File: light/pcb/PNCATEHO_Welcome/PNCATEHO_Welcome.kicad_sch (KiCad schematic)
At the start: 51 parts, among them J1 USB_C_Receptacle_USB2.0, SW11 Boot, SW12 Reset, U1 RP2040, U2 RT9013-33GB, U3 W25Q32JVSSIQ, U4 USBLC6-2SC6, Y1 12MHz

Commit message: clear sch
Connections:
- net RP2040_D+: no longer names the net of R6.2, U1.47 (USB_DP)
- net RP2040_D-: no longer names the net of R7.2, U1.46 (USB_DM)
- net USB_PROTECTED_D+ renamed USB_DP
- net USB_PROTECTED_D- renamed USB_DM
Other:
- note added: "Button"
- note added: "Decoupling capacitor"
- note added: "ESD"
- note added: "Flash"
- note added: "MCU Led"
- note added: "Test Point"
- note removed: "Control"
- note removed: "Decoupling capacitors"
- note removed: "Flash Memory"
- note removed: "Led"
- moved on the sheet: C1, C10, C11, C12, C13, C14, C15, C16, C17, C2, C3, C4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

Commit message: add led
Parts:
- added D10, D11, D12, D3, D4, D5, D6, D7, D8, D9: LED_WS2812-2020, PNCATEHO:WS2812-2020-2.00mmx2.20mm, symbol ws2812:LED_WS2812-2020
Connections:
- net +5V: now also D10.4 (VDD), D11.4 (VDD), D12.4 (VDD), D3.4 (VDD), D4.4 (VDD), D5.4 (VDD), D6.4 (VDD), D7.4 (VDD), D8.4 (VDD), D9.4 (VDD)
- net GND: now also D10.2 (GND), D11.2 (GND), D12.2 (GND), D3.2 (GND), D4.2 (GND), D5.2 (GND), D6.2 (GND), D7.2 (GND), D8.2 (GND), D9.2 (GND)
- net LED: now reaches U1.36 (GPIO24)
- net LED: now also D6.1 (DO)
- new net: D3.1 (DO), D6.3 (DI)
- new net: D3.3 (DI), D4.1 (DO)
- new net: D4.3 (DI), D5.1 (DO)
- new net: D5.3 (DI), D7.1 (DO)
- new net: D10.3 (DI), D11.1 (DO)
- new net: D11.3 (DI), D12.1 (DO)
- new net: D10.1 (DO), D9.3 (DI)
- new net: D7.3 (DI), D8.1 (DO)
- new net: D8.3 (DI), D9.1 (DO)

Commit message: fix sh
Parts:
- removed D10, D11, D12, D3, D4, D5, D6, D7, D8, D9: LED_WS2812-2020, PNCATEHO:WS2812-2020-2.00mmx2.20mm, symbol ws2812:LED_WS2812-2020
- added D10, D11, D12, D3, D4, D5, D6, D7, D8, D9: ~, PNCATEHO:WS2812-2020-2.00mmx2.20mm, symbol PNCATEHO:LED_WS2812-2020
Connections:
- net +5V: now also D10.4 (VDD), D11.4 (VDD), D12.4 (VDD), D3.4 (VDD), D4.4 (VDD), D5.4 (VDD), D6.4 (VDD), D7.4 (VDD), D8.4 (VDD), D9.4 (VDD)
- net GND: now also D10.2 (GND), D11.2 (GND), D12.2 (GND), D3.2 (GND), D4.2 (GND), D5.2 (GND), D6.2 (GND), D7.2 (GND), D8.2 (GND), D9.2 (GND)
- net LED: now also D3.3 (DI)
- new net: D8.1 (DO), D9.3 (DI)
- new net: D7.1 (DO), D8.3 (DI)
- new net: D5.1 (DO), D6.3 (DI)
- new net: D4.1 (DO), D5.3 (DI)
- new net: D6.1 (DO), D7.3 (DI)
- new net: D10.3 (DI), D9.1 (DO)
- new net: D3.1 (DO), D4.3 (DI)
- new net: D10.1 (DO), D11.3 (DI)
- new net: D11.1 (DO), D12.3 (DI)

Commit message: PNCATEHO Welcome RGB routing
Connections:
- net LED: now also U1.37 (GPIO25); no longer U1.36 (GPIO24)
- net STATE_LED: now also U1.36 (GPIO24); no longer U1.37 (GPIO25)

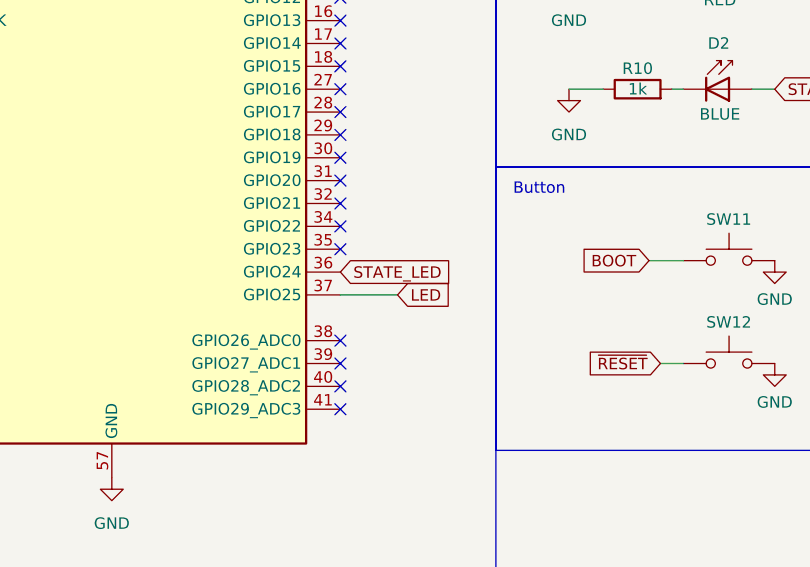
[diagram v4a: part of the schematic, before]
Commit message: Return state led to GPIO25
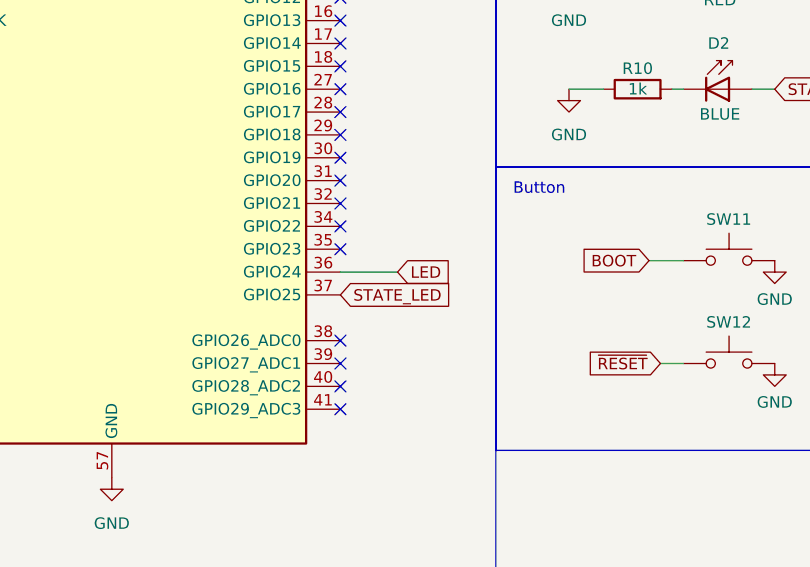
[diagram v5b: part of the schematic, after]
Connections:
- net LED: now also U1.36 (GPIO24); no longer U1.37 (GPIO25)
- net STATE_LED: now also U1.37 (GPIO25); no longer U1.36 (GPIO24)
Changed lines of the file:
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@@
+	(wire
+		(pts
+			(xy 92.71 152.4) (xy 86.36 152.4)
+		)
+		(stroke
+			(width 0)
+			(type default)
+		)
+	)
 	(wire
 		(pts
@@
 	(wire
 		(pts
-			(xy 92.71 154.94) (xy 86.36 154.94)
-		)
-		(stroke
-			(width 0)
-			(type default)
-		)
-	)
-	(wire
-		(pts
 			(xy 226.06 132.08) (xy 226.06 137.16)
 		)
@@
 	(global_label "LED"
 		(shape input)
-		(at 92.71 154.94 0)
-		(fields_autoplaced yes)
-		(effects
-			(font
-				(size 1.27 1.27)
-			)
-			(justify left)
-		)
-		(property "Intersheetrefs" "${INTERSHEET_REFS}"
-			(at 99.1423 154.94 0)
+		(at 92.71 152.4 0)
+		(fields_autoplaced yes)
+		(effects
+			(font
+				(size 1.27 1.27)
+			)
+			(justify left)
+		)
+		(property "Intersheetrefs" "${INTERSHEET_REFS}"
+			(at 99.1423 152.4 0)
 			(effects
 				(font
@@
 	(global_label "STATE_LED"
 		(shape input)
-		(at 86.36 152.4 0)
-		(fields_autoplaced yes)
-		(effects
-			(font
-				(size 1.27 1.27)
-			)
-			(justify left)
-		)
-		(property "Intersheetrefs" "${INTERSHEET_REFS}"
-			(at 99.1422 152.4 0)
-			(effects
-				(font
+		(at 86.36 154.94 0)
+		(fields_autoplaced yes)
+		(effects
+			(font
+				(size 1.27 1.27)
+			)
+			(justify left)
+		)
+		(property "Intersheetrefs" "${INTERSHEET_REFS}"
+			(at 99.1422 154.94 0)
+			(effects
+				(font

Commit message: update scheme
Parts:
- added J2: Conn_01x10, PNCATEHO:JST_GH_SM10B-GHS-TB_1x10-1MP_P1.25mm_Horizontal, symbol PNCATEHO:Conn_01x10
- U2: footprint PNCATEHO:SOT-23-5_L3.0-W1.7-P0.95-LS2.8-BL -> PNCATEHO:SOT-23-5_HandSoldering
- U4: footprint PNCATEHO:SOT-23-6_Handsoldering_REV -> PNCATEHO:SOT-23-6_Handsoldering
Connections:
- net +3V3: now also J2.1 (Pin_1)
- net GND: now also J2.10 (Pin_10)
- net GPIO1: now reaches U1.13 (GPIO10)
- net GPIO1: now also J2.2 (Pin_2)
- net GPIO2: now reaches U1.14 (GPIO11)
- net GPIO2: now also J2.3 (Pin_3)
- net GPIO3: now reaches U1.15 (GPIO12)
- net GPIO3: now also J2.4 (Pin_4)
- net GPIO4: now reaches U1.16 (GPIO13)
- net GPIO4: now also J2.5 (Pin_5)
- net GPIO5: now reaches U1.17 (GPIO14)
- net GPIO5: now also J2.6 (Pin_6)
- net GPIO6: now reaches U1.18 (GPIO15)
- net GPIO6: now also J2.7 (Pin_7)
- net GPIO7: now reaches U1.27 (GPIO16)
- net GPIO7: now also J2.8 (Pin_8)
- net GPIO8: now reaches U1.28 (GPIO17)
- net GPIO8: now also J2.9 (Pin_9)
- no-connect marks 21 -> 13

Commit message: update footprint
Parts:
- F1: footprint PNCATEHO:Fuse_0805_2012Metric -> PNCATEHO:Fuse_0805_2012Metric_Pad1.15x1.40mm_HandSolder
- TP1: footprint PNCATEHO:TestPoint_Pad_D2.0mm -> PNCATEHO:TestPoint_Pad_1.0x1.0mm
- TP2, TP3, TP4: footprint PNCATEHO:TestPoint_Pad_D2.0mm -> PNCATEHO:TestPoint_Pad_D1.0mm
- U1: footprint PNCATEHO:RP2040-QFN-56 -> PNCATEHO:QFN-56-1EP_7x7mm_P0.4mm_EP3.2x3.2mm_ThermalVias
- U3: footprint PNCATEHO:SOIC127P790X216-8N -> PNCATEHO:SOIC-8_5.3x5.3mm_P1.27mm
- Y1: footprint PNCATEHO:Crystal_SMD_3225-4Pin_3.2x2.5mm -> PNCATEHO:Crystal_SMD_3225-4Pin_3.2x2.5mm_HandSoldering
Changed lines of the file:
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@@
 			)
 		)
-		(property "Footprint" "PNCATEHO:TestPoint_Pad_D2.0mm"
+		(property "Footprint" "PNCATEHO:TestPoint_Pad_D1.0mm"
 			(at 185.42 137.16 0)
 			(effects
@@
 			)
 		)
-		(property "Footprint" "PNCATEHO:RP2040-QFN-56"
+		(property "Footprint" "PNCATEHO:QFN-56-1EP_7x7mm_P0.4mm_EP3.2x3.2mm_ThermalVias"
 			(at 60.96 129.54 0)
 			(effects
@@
 			)
 		)
-		(property "Footprint" "PNCATEHO:TestPoint_Pad_D2.0mm"
+		(property "Footprint" "PNCATEHO:TestPoint_Pad_1.0x1.0mm"
 			(at 166.37 137.16 0)
 			(effects
@@
 			)
 		)
-		(property "Footprint" "PNCATEHO:Fuse_0805_2012Metric"
+		(property "Footprint" "PNCATEHO:Fuse_0805_2012Metric_Pad1.15x1.40mm_HandSolder"
 			(at 54.61 24.13 0)
 			(effects
@@
 			)
 		)
-		(property "Footprint" "PNCATEHO:TestPoint_Pad_D2.0mm"
+		(property "Footprint" "PNCATEHO:TestPoint_Pad_D1.0mm"
 			(at 184.15 121.92 0)
 			(effects
@@
 			)
 		)
-		(property "Footprint" "PNCATEHO:Crystal_SMD_3225-4Pin_3.2x2.5mm"
+		(property "Footprint" "PNCATEHO:Crystal_SMD_3225-4Pin_3.2x2.5mm_HandSoldering"
 			(at 54.61 201.93 0)
 			(effects
@@
 			)
 		)
-		(property "Footprint" "PNCATEHO:SOIC127P790X216-8N"
+		(property "Footprint" "PNCATEHO:SOIC-8_5.3x5.3mm_P1.27mm"
 			(at 158.75 95.25 0)
 			(effects
@@
 			)
 		)
-		(property "Footprint" "PNCATEHO:TestPoint_Pad_D2.0mm"
+		(property "Footprint" "PNCATEHO:TestPoint_Pad_D1.0mm"
 			(at 165.1 121.92 0)
 			(effects

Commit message: update sh
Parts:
- added J3: Conn_01x10, PNCATEHO:JST_GH_SM10B-GHS-TB_1x10-1MP_P1.25mm_Horizontal, symbol PNCATEHO:Conn_01x10
- added J4, J5: Conn_01x05, symbol PNCATEHO:Conn_01x05
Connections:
- net +3V3: now also J3.1 (Pin_1), J4.1 (Pin_1)
- net GND: now also J3.10 (Pin_10), J5.5 (Pin_5)
- net GPIO1: now also J3.2 (Pin_2), J4.2 (Pin_2)
- net GPIO2: now also J3.3 (Pin_3), J4.3 (Pin_3)
- net GPIO3: now also J3.4 (Pin_4), J4.4 (Pin_4)
- net GPIO4: now also J3.5 (Pin_5), J4.5 (Pin_5)
- net GPIO5: now also J3.6 (Pin_6), J5.1 (Pin_1)
- net GPIO6: now also J3.7 (Pin_7), J5.2 (Pin_2)
- net GPIO7: now also J3.8 (Pin_8), J5.3 (Pin_3)
- net GPIO8: now also J3.9 (Pin_9), J5.4 (Pin_4)
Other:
- note added: "Dev Board"
- note added: "JST"
- note added: "Per key LED"
- moved on the sheet: D10, D11, D12, D3, D4, D5, D6, D7, D8, D9, J2
